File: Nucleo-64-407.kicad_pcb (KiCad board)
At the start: 2 copper layers, 70 x 81 mm, 74 parts, among them J1 SWD, J3 USB_B_Micro, J4 Serial 0, J5 EXP1, J6 EXP2, J7 EXP3, J8 EXP4, SW1 RESET, SW2 BOOT, U1 STM32F407VETx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

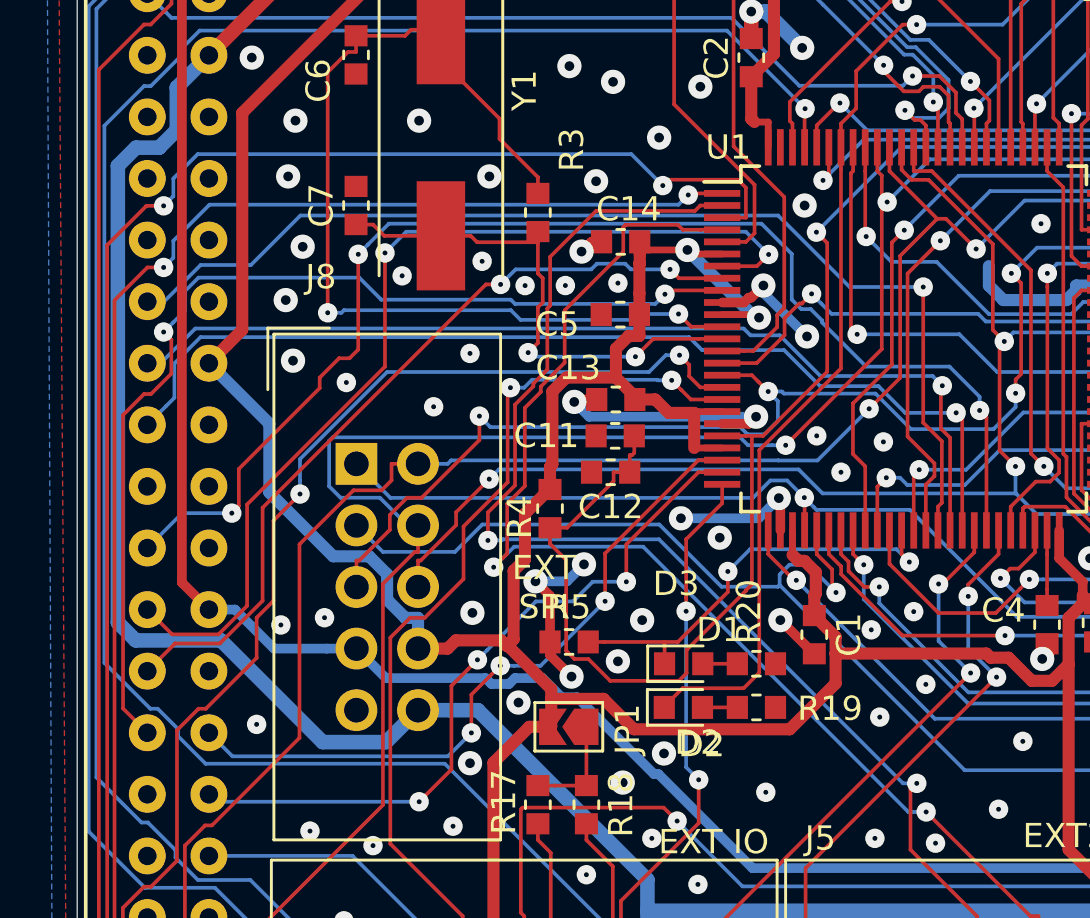
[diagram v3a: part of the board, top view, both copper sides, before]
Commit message: Added 3.3V LDO, updated TC connectors to 6 pins. Re-arranged the layout.
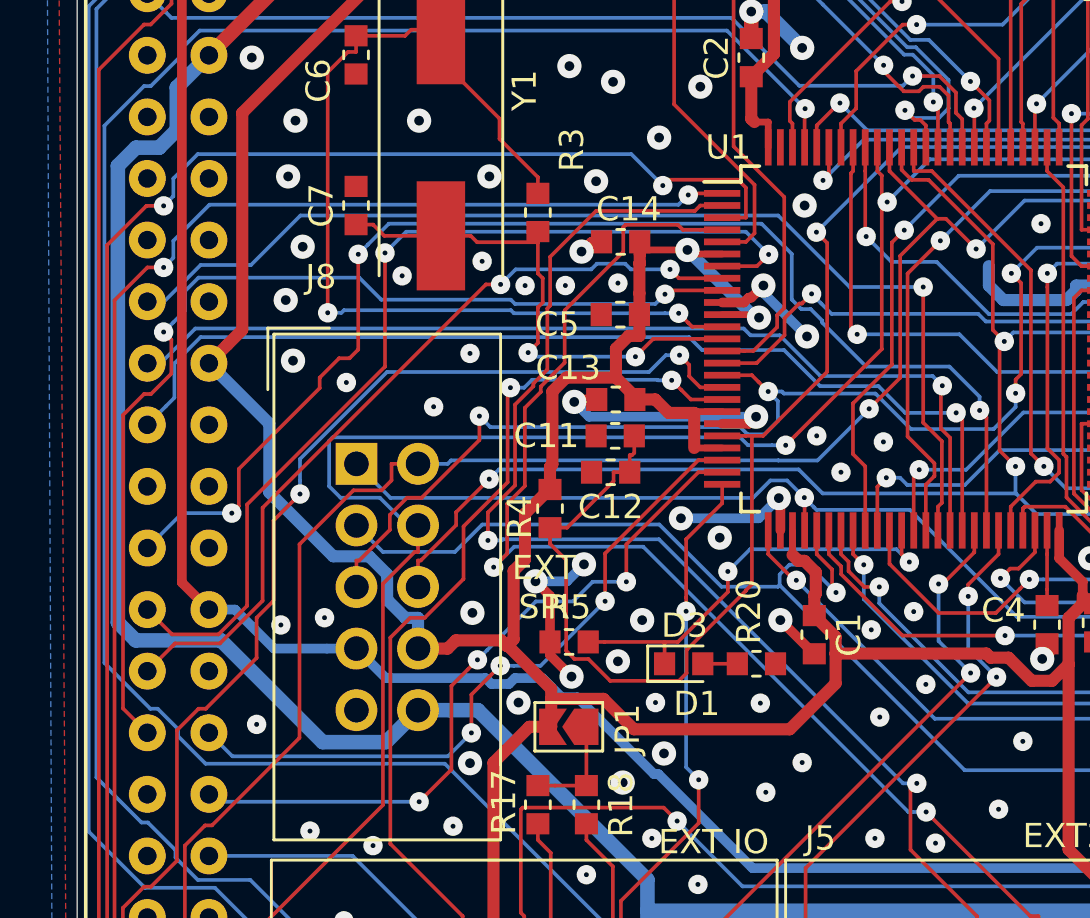
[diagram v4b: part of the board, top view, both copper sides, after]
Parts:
- removed D2: B0, PrntrBoardV1:D_0603_1608Metric
- removed R19: 470, PrntrBoardV1:R_0603_1608Metric
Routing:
- net /BOOT0: track 63.2 -> 35.6 mm
- net Net-(D2-Pad2): track 1.44 -> 0.00 mm
- net GND: vias 183 -> 186
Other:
- board text removed: "D2"
